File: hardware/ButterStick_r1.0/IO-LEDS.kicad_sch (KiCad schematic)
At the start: 20 parts, among them Q1 Q_NMOS_GSD, Q2 Q_NMOS_GSD, Q3 Q_NMOS_GSD

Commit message: hw.r1d0: Review complete, gerbers generated
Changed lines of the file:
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@@
 (kicad_sch (version 20200618) (host eeschema "5.99.0-unknown-73168a9~101~ubuntu18.04.1")
-  (page 1 18)
+  (page 5 18)
   (paper "A4")
   (title_block
     (title "ButterStick")
-    (date "2020-07-16")
+    (date "2020-07-17")
     (rev "r1.0")
     (company "GsD")
@@
     (stroke (width 0) (type solid) (color 0 0 0 0))
   )
-  (bus (pts (xy 110.49 106.68) (xy 118.11 106.68))
+  (bus (pts (xy 110.49 106.68) (xy 123.19 106.68))
     (stroke (width 0) (type solid) (color 0 0 0 0))
   )
@@
     (stroke (width 0) (type solid) (color 0 0 0 0))
   )
-  (bus (pts (xy 118.11 106.68) (xy 128.27 106.68))
+  (bus (pts (xy 123.19 106.68) (xy 128.27 106.68))
     (stroke (width 0) (type solid) (color 0 0 0 0))
   )
@@
     (stroke (width 0) (type solid) (color 0 0 0 0))
   )
-  (bus (pts (xy 128.27 106.68) (xy 135.89 106.68))
-    (stroke (width 0) (type solid) (color 0 0 0 0))
-  )
-  (bus (pts (xy 135.89 106.68) (xy 146.05 106.68))
-    (stroke (width 0) (type solid) (color 0 0 0 0))
-  )
-  (bus (pts (xy 146.05 106.68) (xy 158.75 106.68))
-    (stroke (width 0) (type solid) (color 0 0 0 0))
-  )
-  (bus (pts (xy 158.75 106.68) (xy 171.45 106.68))
+  (bus (pts (xy 128.27 106.68) (xy 140.97 106.68))
+    (stroke (width 0) (type solid) (color 0 0 0 0))
+  )
+  (bus (pts (xy 140.97 106.68) (xy 153.67 106.68))
+    (stroke (width 0) (type solid) (color 0 0 0 0))
+  )
+  (bus (pts (xy 153.67 106.68) (xy 163.83 106.68))
     (stroke (width 0) (type solid) (color 0 0 0 0))
   )
@@
     (stroke (width 0) (type solid) (color 0 0 0 0))
   )
-  (bus (pts (xy 171.45 106.68) (xy 181.61 106.68))
+  (bus (pts (xy 163.83 106.68) (xy 176.53 106.68))
     (stroke (width 0) (type solid) (color 0 0 0 0))
   )
@@
     (stroke (width 0) (type solid) (color 0 0 0 0))
   )
-  (bus (pts (xy 181.61 106.68) (xy 194.31 106.68))
-    (stroke (width 0) (type solid) (color 0 0 0 0))
-  )
+  (bus (pts (xy 176.53 106.68) (xy 189.23 106.68))
+    (stroke (width 0) (type solid) (color 0 0 0 0))
+  )
+  (bus (pts (xy 189.23 106.68) (xy 194.31 106.68))
+    (stroke (width 0) (type solid) (color 0 0 0 0))
+  )

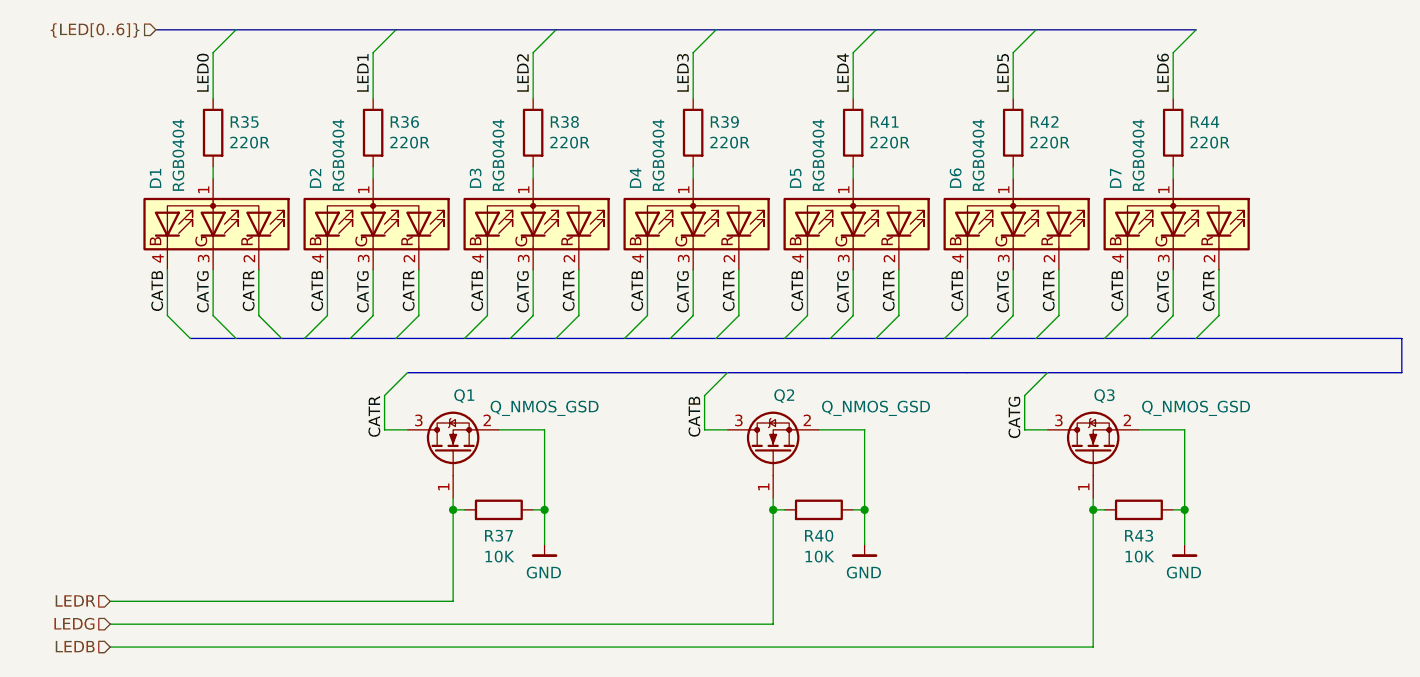
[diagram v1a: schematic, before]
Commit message: hw.r1d0: Update BOM fieids in schematic.
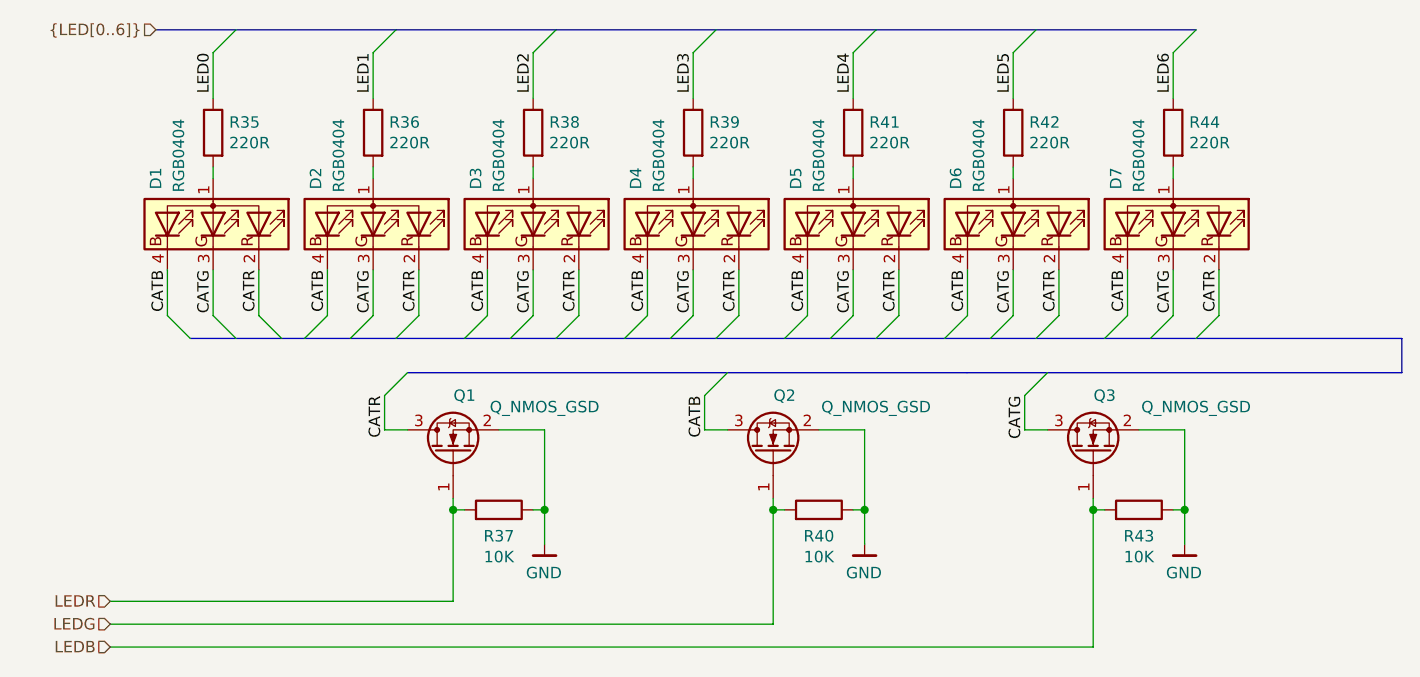
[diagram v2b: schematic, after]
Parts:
- D1, D2, D3, D4, D5, D6, D7: MFG Foshan NationStar -> (none); Mfg (none) -> Foshan NationStar
- Q1, Q2, Q3: Mfg (none) -> Nexperia; PN (none) -> 2N7002PW\,115
- R35, R36, R38, R39, R41, R42, R44: Mfg (none) -> Yageo; PN (none) -> RC0402FR-07220RL
- R37, R40, R43: Mfg (none) -> Yageo; PN (none) -> RC0402FR-0710KL
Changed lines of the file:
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@@
 (kicad_sch (version 20200618) (host eeschema "5.99.0-unknown-73168a9~101~ubuntu18.04.1")
-  (page 5 18)
+  (page 1 18)
   (paper "A4")
   (title_block
@@
     (stroke (width 0) (type solid) (color 0 0 0 0))
   )
-  (bus (pts (xy 110.49 106.68) (xy 123.19 106.68))
+  (bus (pts (xy 110.49 106.68) (xy 118.11 106.68))
     (stroke (width 0) (type solid) (color 0 0 0 0))
   )
@@
     (stroke (width 0) (type solid) (color 0 0 0 0))
   )
-  (bus (pts (xy 123.19 106.68) (xy 128.27 106.68))
+  (bus (pts (xy 118.11 106.68) (xy 128.27 106.68))
     (stroke (width 0) (type solid) (color 0 0 0 0))
   )
@@
     (stroke (width 0) (type solid) (color 0 0 0 0))
   )
-  (bus (pts (xy 128.27 106.68) (xy 140.97 106.68))
-    (stroke (width 0) (type solid) (color 0 0 0 0))
-  )
-  (bus (pts (xy 140.97 106.68) (xy 153.67 106.68))
-    (stroke (width 0) (type solid) (color 0 0 0 0))
-  )
-  (bus (pts (xy 153.67 106.68) (xy 163.83 106.68))
+  (bus (pts (xy 128.27 106.68) (xy 135.89 106.68))
+    (stroke (width 0) (type solid) (color 0 0 0 0))
+  )
+  (bus (pts (xy 135.89 106.68) (xy 146.05 106.68))
+    (stroke (width 0) (type solid) (color 0 0 0 0))
+  )
+  (bus (pts (xy 146.05 106.68) (xy 158.75 106.68))
+    (stroke (width 0) (type solid) (color 0 0 0 0))
+  )
+  (bus (pts (xy 158.75 106.68) (xy 171.45 106.68))
     (stroke (width 0) (type solid) (color 0 0 0 0))
   )
@@
     (stroke (width 0) (type solid) (color 0 0 0 0))
   )
-  (bus (pts (xy 163.83 106.68) (xy 176.53 106.68))
+  (bus (pts (xy 171.45 106.68) (xy 181.61 106.68))
     (stroke (width 0) (type solid) (color 0 0 0 0))
   )
@@
     (stroke (width 0) (type solid) (color 0 0 0 0))
   )
-  (bus (pts (xy 176.53 106.68) (xy 189.23 106.68))
-    (stroke (width 0) (type solid) (color 0 0 0 0))
-  )
-  (bus (pts (xy 189.23 106.68) (xy 194.31 106.68))
+  (bus (pts (xy 181.61 106.68) (xy 194.31 106.68))
     (stroke (width 0) (type solid) (color 0 0 0 0))
   )
@@
       (effects (font (size 1.27 1.27)) hide)
     )
+    (property "Mfg" "Yageo" (id 4) (at 90.17 83.82 0)
+      (effects (font (size 1.27 1.27)) hide)
+    )
+    (property "PN" "RC0402FR-07220RL" (id 4) (at 90.17 83.82 0)
+      (effects (font (size 1.27 1.27)) hide)
+    )
   )
   (symbol (lib_id "Device:R") (at 107.95 83.82 0) (mirror y) (unit 1)
@@
     )
     (property "Datasheet" "~" (id 3) (at 107.95 83.82 0)
+      (effects (font (size 1.27 1.27)) hide)
+    )
+    (property "Mfg" "Yageo" (id 4) (at 107.95 83.82 0)
+      (effects (font (size 1.27 1.27)) hide)
+    )
+    (property "PN" "RC0402FR-07220RL" (id 4) (at 107.95 83.82 0)
       (effects (font (size 1.27 1.27)) hide)
     )
@@
       (effects (font (size 1.27 1.27)) hide)
     )
+    (property "Mfg" "Yageo" (id 4) (at 121.92 125.73 0)
+      (effects (font (size 1.27 1.27)) hide)
+    )
+    (property "PN" "RC0402FR-0710KL" (id 4) (at 121.92 125.73 0)
+      (effects (font (size 1.27 1.27)) hide)
+    )
   )
   (symbol (lib_id "Device:R") (at 125.73 83.82 0) (mirror y) (unit 1)
@@
       (effects (font (size 1.27 1.27)) hide)
     )
+    (property "Mfg" "Yageo" (id 4) (at 125.73 83.82 0)
+      (effects (font (size 1.27 1.27)) hide)
+    )
+    (property "PN" "RC0402FR-07220RL" (id 4) (at 125.73 83.82 0)
+      (effects (font (size 1.27 1.27)) hide)
+    )
   )
   (symbol (lib_id "Device:R") (at 143.51 83.82 0) (mirror y) (unit 1)
@@
     )
     (property "Datasheet" "~" (id 3) (at 143.51 83.82 0)
+      (effects (font (size 1.27 1.27)) hide)
+    )
+    (property "Mfg" "Yageo" (id 4) (at 143.51 83.82 0)
+      (effects (font (size 1.27 1.27)) hide)
+    )
+    (property "PN" "RC0402FR-07220RL" (id 4) (at 143.51 83.82 0)
       (effects (font (size 1.27 1.27)) hide)
     )
@@
       (effects (font (size 1.27 1.27)) hide)
     )
+    (property "Mfg" "Yageo" (id 4) (at 157.48 125.73 0)
+      (effects (font (size 1.27 1.27)) hide)
+    )
+    (property "PN" "RC0402FR-0710KL" (id 4) (at 157.48 125.73 0)
+      (effects (font (size 1.27 1.27)) hide)
+    )
   )
   (symbol (lib_id "Device:R") (at 161.29 83.82 0) (mirror y) (unit 1)
@@
       (effects (font (size 1.27 1.27)) hide)
     )
+    (property "Mfg" "Yageo" (id 4) (at 161.29 83.82 0)
+      (effects (font (size 1.27 1.27)) hide)
+    )
+    (property "PN" "RC0402FR-07220RL" (id 4) (at 161.29 83.82 0)
+      (effects (font (size 1.27 1.27)) hide)
+    )
   )
   (symbol (lib_id "Device:R") (at 179.07 83.82 0) (mirror y) (unit 1)
@@
     )
     (property "Datasheet" "~" (id 3) (at 179.07 83.82 0)
+      (effects (font (size 1.27 1.27)) hide)
+    )
+    (property "Mfg" "Yageo" (id 4) (at 179.07 83.82 0)
+      (effects (font (size 1.27 1.27)) hide)
+    )
+    (property "PN" "RC0402FR-07220RL" (id 4) (at 179.07 83.82 0)
       (effects (font (size 1.27 1.27)) hide)
     )
@@
       (effects (font (size 1.27 1.27)) hide)
     )
+    (property "Mfg" "Yageo" (id 4) (at 193.04 125.73 0)
+      (effects (font (size 1.27 1.27)) hide)
+    )
+    (property "PN" "RC0402FR-0710KL" (id 4) (at 193.04 125.73 0)
+      (effects (font (size 1.27 1.27)) hide)
+    )
   )
   (symbol (lib_id "Device:R") (at 196.85 83.82 0) (mirror y) (unit 1)
@@
     )
     (property "Datasheet" "~" (id 3) (at 196.85 83.82 0)
+      (effects (font (size 1.27 1.27)) hide)
+    )
+    (property "Mfg" "Yageo" (id 4) (at 196.85 83.82 0)
+      (effects (font (size 1.27 1.27)) hide)
+    )
+    (property "PN" "RC0402FR-07220RL" (id 4) (at 196.85 83.82 0)
       (effects (font (size 1.27 1.27)) hide)
     )
@@
       (effects (font (size 1.27 1.27)) hide)
     )
+    (property "Mfg" "Nexperia" (id 4) (at 116.84 119.38 0)
+      (effects (font (size 1.27 1.27)) hide)
+    )
+    (property "PN" "2N7002PW\\,115" (id 5) (at 116.84 119.38 0)
+      (effects (font (size 1.27 1.27)) hide)
+    )
   )
   (symbol (lib_name "Device:Q_NMOS_GSD_2") (lib_id "Device:Q_NMOS_GSD") (at 152.4 119.38 90) (unit 1)
@@
       (effects (font (size 1.27 1.27)) hide)
     )
+    (property "Mfg" "Nexperia" (id 4) (at 152.4 119.38 0)
+      (effects (font (size 1.27 1.27)) hide)
+    )
+    (property "PN" "2N7002PW\\,115" (id 5) (at 152.4 119.38 0)
+      (effects (font (size 1.27 1.27)) hide)
+    )
   )
   (symbol (lib_id "Device:Q_NMOS_GSD") (at 187.96 119.38 90) (unit 1)
@@
       (effects (font (size 1.27 1.27)) hide)
     )
+    (property "Mfg" "Nexperia" (id 4) (at 187.96 119.38 0)
+      (effects (font (size 1.27 1.27)) hide)
+    )
+    (property "PN" "2N7002PW\\,115" (id 5) (at 187.96 119.38 0)
+      (effects (font (size 1.27 1.27)) hide)
+    )
   )
   (symbol (lib_id "Device:LED_ARGB") (at 90.17 93.98 270) (mirror x) (unit 1)
@@
       (effects (font (size 1.27 1.27)) hide)
     )
-    (property "MFG" "Foshan NationStar" (id 4) (at 90.17 93.98 0)
+    (property "MFG" "" (id 4) (at 90.17 93.98 0)
       (effects (font (size 1.27 1.27)) hide)
     )
     (property "PN" "FC-B1010RGBT-HG" (id 5) (at 90.17 93.98 0)
+      (effects (font (size 1.27 1.27)) hide)
+    )
+    (property "Mfg" "Foshan NationStar" (id 4) (at 90.17 93.98 0)
       (effects (font (size 1.27 1.27)) hide)
     )
@@
       (effects (font (size 1.27 1.27)) hide)
     )
-    (property "MFG" "Foshan NationStar" (id 4) (at 107.95 93.98 0)
+    (property "MFG" "" (id 4) (at 107.95 93.98 0)
       (effects (font (size 1.27 1.27)) hide)
     )
     (property "PN" "FC-B1010RGBT-HG" (id 5) (at 107.95 93.98 0)
+      (effects (font (size 1.27 1.27)) hide)
+    )
+    (property "Mfg" "Foshan NationStar" (id 4) (at 107.95 93.98 0)
       (effects (font (size 1.27 1.27)) hide)
     )
@@
       (effects (font (size 1.27 1.27)) hide)
     )
-    (property "MFG" "Foshan NationStar" (id 4) (at 125.73 93.98 0)
+    (property "MFG" "" (id 4) (at 125.73 93.98 0)
       (effects (font (size 1.27 1.27)) hide)
     )
     (property "PN" "FC-B1010RGBT-HG" (id 5) (at 125.73 93.98 0)
+      (effects (font (size 1.27 1.27)) hide)
+    )
+    (property "Mfg" "Foshan NationStar" (id 4) (at 125.73 93.98 0)
       (effects (font (size 1.27 1.27)) hide)
     )
@@
       (effects (font (size 1.27 1.27)) hide)
     )
-    (property "MFG" "Foshan NationStar" (id 4) (at 143.51 93.98 0)
+    (property "MFG" "" (id 4) (at 143.51 93.98 0)
       (effects (font (size 1.27 1.27)) hide)
     )
     (property "PN" "FC-B1010RGBT-HG" (id 5) (at 143.51 93.98 0)
+      (effects (font (size 1.27 1.27)) hide)
+    )
+    (property "Mfg" "Foshan NationStar" (id 4) (at 143.51 93.98 0)
       (effects (font (size 1.27 1.27)) hide)
     )
@@
       (effects (font (size 1.27 1.27)) hide)
     )
-    (property "MFG" "Foshan NationStar" (id 4) (at 161.29 93.98 0)
+    (property "MFG" "" (id 4) (at 161.29 93.98 0)
       (effects (font (size 1.27 1.27)) hide)
     )
     (property "PN" "FC-B1010RGBT-HG" (id 5) (at 161.29 93.98 0)
+      (effects (font (size 1.27 1.27)) hide)
+    )
+    (property "Mfg" "Foshan NationStar" (id 4) (at 161.29 93.98 0)
       (effects (font (size 1.27 1.27)) hide)
     )
@@
       (effects (font (size 1.27 1.27)) hide)
     )
-    (property "MFG" "Foshan NationStar" (id 4) (at 179.07 93.98 0)
+    (property "MFG" "" (id 4) (at 179.07 93.98 0)
       (effects (font (size 1.27 1.27)) hide)
     )
     (property "PN" "FC-B1010RGBT-HG" (id 5) (at 179.07 93.98 0)
+      (effects (font (size 1.27 1.27)) hide)
+    )
+    (property "Mfg" "Foshan NationStar" (id 4) (at 179.07 93.98 0)
       (effects (font (size 1.27 1.27)) hide)
     )
@@
       (effects (font (size 1.27 1.27)) hide)
     )
-    (property "MFG" "Foshan NationStar" (id 4) (at 196.85 93.98 0)
+    (property "MFG" "" (id 4) (at 196.85 93.98 0)
       (effects (font (size 1.27 1.27)) hide)
     )
@@
       (effects (font (size 1.27 1.27)) hide)
     )
+    (property "Mfg" "Foshan NationStar" (id 4) (at 196.85 93.98 0)
+      (effects (font (size 1.27 1.27)) hide)
+    )
